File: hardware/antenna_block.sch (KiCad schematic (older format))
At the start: 28 parts

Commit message: added rx/tx wm8731 (adc/dac)
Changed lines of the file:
@@
 	2950 3100 3050 3100
 Wire Wire Line
-	3250 3100 3500 3100
+	3250 3100 3400 3100
+Wire Wire Line
+	3400 3100 3500 3100
 Wire Wire Line
 	3400 3100 3400 3200
 Connection ~ 3400 3100
 Wire Wire Line
-	3700 3100 3900 3100
+	3700 3100 3800 3100
+Wire Wire Line
+	3800 3100 3900 3100
 Wire Wire Line
 	3800 3200 3800 3100
@@
 	3400 3400 3400 3550
 Wire Wire Line
-	2600 3550 4200 3550
+	2600 3550 3400 3550
+Wire Wire Line
+	3400 3550 3800 3550
+Wire Wire Line
+	3800 3550 4200 3550
 Wire Wire Line
 	3800 3550 3800 3400
@@
 Connection ~ 3400 3550
 Wire Wire Line
-	4100 3100 4350 3100
+	4100 3100 4200 3100
+Wire Wire Line
+	4200 3100 4350 3100
 Wire Wire Line
 	4200 3100 4200 3200
@@
 	4400 3900 4400 4100
 Wire Wire Line
-	4400 3900 4650 3900
+	4400 3900 4550 3900
+Wire Wire Line
+	4550 3900 4650 3900
 Wire Wire Line
 	4550 3900 4550 4550
@@
 	5950 3850 5650 3850
 Wire Wire Line
-	5650 3650 5650 3900
+	5650 3650 5650 3850
+Wire Wire Line
+	5650 3850 5650 3900
 Connection ~ 4550 3900
 Connection ~ 5650 3850
@@
 	4650 3900 4650 3650
 Wire Wire Line
-	4950 3650 4950 3900
-Wire Wire Line
-	5350 3650 5350 3900
+	4950 3650 4950 3700
+Wire Wire Line
+	4950 3700 4950 3900
+Wire Wire Line
+	5350 3650 5350 3800
+Wire Wire Line
+	5350 3800 5350 3900
 Wire Wire Line
 	4650 4100 4650 4200
 Wire Wire Line
-	4650 4200 5650 4200
+	4650 4200 4950 4200
+Wire Wire Line
+	4950 4200 5150 4200
+Wire Wire Line
+	5150 4200 5350 4200
+Wire Wire Line
+	5350 4200 5650 4200
 Wire Wire Line
 	5650 4200 5650 4100
@@
 $EndComp
 Wire Wire Line
-	5650 3100 7750 3100
+	5650 3100 7200 3100
+Wire Wire Line
+	7200 3100 7400 3100
+Wire Wire Line
+	7400 3100 7750 3100
 Connection ~ 7200 3100
 Connection ~ 7400 3100
 Wire Wire Line
-	7950 3100 8150 3100
+	7950 3100 8050 3100
+Wire Wire Line
+	8050 3100 8150 3100
 Wire Wire Line
 	8050 3050 8050 3100
@@
 	7200 3450 7200 3300
 Wire Wire Line
-	6850 3450 7400 3450
+	6850 3450 6900 3450
+Wire Wire Line
+	6900 3450 7200 3450
+Wire Wire Line
+	7200 3450 7400 3450
 Connection ~ 7200 3450
 Connection ~ 6900 3450
@@
 	7800 3350 7800 3750
 Wire Wire Line
-	7800 3750 6900 3750
+	7800 3750 7400 3750
+Wire Wire Line
+	7400 3750 7200 3750
+Wire Wire Line
+	7200 3750 6900 3750
 Wire Wire Line
 	7400 3750 7400 3650

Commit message: Added TX chain schematic block and Vin netlist for input power_flag
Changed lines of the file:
@@
 $Descr A4 11693 8268
 encoding utf-8
-Sheet 3 4
+Sheet 3 5
 Title "Antenna block, SWR-meter and RXTX switch"
 Date "2016-09-22"
@@
 	2950 3100 3050 3100
 Wire Wire Line
-	3250 3100 3400 3100
-Wire Wire Line
-	3400 3100 3500 3100
+	3250 3100 3500 3100
 Wire Wire Line
 	3400 3100 3400 3200
 Connection ~ 3400 3100
 Wire Wire Line
-	3700 3100 3800 3100
-Wire Wire Line
-	3800 3100 3900 3100
+	3700 3100 3900 3100
 Wire Wire Line
 	3800 3200 3800 3100
@@
 	3400 3400 3400 3550
 Wire Wire Line
-	2600 3550 3400 3550
-Wire Wire Line
-	3400 3550 3800 3550
-Wire Wire Line
-	3800 3550 4200 3550
+	2600 3550 4200 3550
 Wire Wire Line
 	3800 3550 3800 3400
@@
 Connection ~ 3400 3550
 Wire Wire Line
-	4100 3100 4200 3100
-Wire Wire Line
-	4200 3100 4350 3100
+	4100 3100 4350 3100
 Wire Wire Line
 	4200 3100 4200 3200
@@
 	4400 3900 4400 4100
 Wire Wire Line
-	4400 3900 4550 3900
-Wire Wire Line
-	4550 3900 4650 3900
+	4400 3900 4650 3900
 Wire Wire Line
 	4550 3900 4550 4550
@@
 	5950 3850 5650 3850
 Wire Wire Line
-	5650 3650 5650 3850
-Wire Wire Line
-	5650 3850 5650 3900
+	5650 3650 5650 3900
 Connection ~ 4550 3900
 Connection ~ 5650 3850
@@
 	4650 3900 4650 3650
 Wire Wire Line
-	4950 3650 4950 3700
-Wire Wire Line
-	4950 3700 4950 3900
-Wire Wire Line
-	5350 3650 5350 3800
-Wire Wire Line
-	5350 3800 5350 3900
+	4950 3650 4950 3900
+Wire Wire Line
+	5350 3650 5350 3900
 Wire Wire Line
 	4650 4100 4650 4200
 Wire Wire Line
-	4650 4200 4950 4200
-Wire Wire Line
-	4950 4200 5150 4200
-Wire Wire Line
-	5150 4200 5350 4200
-Wire Wire Line
-	5350 4200 5650 4200
+	4650 4200 5650 4200
 Wire Wire Line
 	5650 4200 5650 4100
@@
 $EndComp
 Wire Wire Line
-	5650 3100 7200 3100
-Wire Wire Line
-	7200 3100 7400 3100
-Wire Wire Line
-	7400 3100 7750 3100
+	5650 3100 7750 3100
 Connection ~ 7200 3100
 Connection ~ 7400 3100
 Wire Wire Line
-	7950 3100 8050 3100
-Wire Wire Line
-	8050 3100 8150 3100
+	7950 3100 8150 3100
 Wire Wire Line
 	8050 3050 8050 3100
@@
 	7200 3450 7200 3300
 Wire Wire Line
-	6850 3450 6900 3450
-Wire Wire Line
-	6900 3450 7200 3450
-Wire Wire Line
-	7200 3450 7400 3450
+	6850 3450 7400 3450
 Connection ~ 7200 3450
 Connection ~ 6900 3450
@@
 	7400 3350 7800 3350
 Wire Wire Line
-	7800 3350 7800 3750
-Wire Wire Line
-	7800 3750 7400 3750
-Wire Wire Line
-	7400 3750 7200 3750
-Wire Wire Line
-	7200 3750 6900 3750
+	7800 3750 7800 3350
+Wire Wire Line
+	6900 3750 7800 3750
 Wire Wire Line
 	7400 3750 7400 3650

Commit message: Added RX chain. also modified and cleand up other schemas
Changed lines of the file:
@@
 $Descr A4 11693 8268
 encoding utf-8
-Sheet 3 5
+Sheet 3 7
 Title "Antenna block, SWR-meter and RXTX switch"
 Date "2016-09-22"
@@
 $EndComp
 $Comp
-L GND #PWR?
+L GND #PWR09
 U 1 1 57E329F5
 P 3800 3550
-F 0 "#PWR?" H 3800 3300 50  0001 C CNN
+F 0 "#PWR09" H 3800 3300 50  0001 C CNN
 F 1 "GND" H 3800 3400 50  0000 C CNN
 F 2 "" H 3800 3550 50  0000 C CNN
@@
 $EndComp
 $Comp
-L +Vlogic #PWR?
+L +Vlogic #PWR010
 U 1 1 57E32A6B
 P 4100 3900
-F 0 "#PWR?" H 4100 3700 50  0001 C CNN
+F 0 "#PWR010" H 4100 3700 50  0001 C CNN
 F 1 "+Vlogic" H 4100 4100 50  0000 C CNN
 F 2 "" H 4100 3900 50  0000 C CNN
@@
 $EndComp
 $Comp
-L GND #PWR?
+L GND #PWR011
 U 1 1 57E32A71
 P 5150 4300
-F 0 "#PWR?" H 5150 4050 50  0001 C CNN
+F 0 "#PWR011" H 5150 4050 50  0001 C CNN
 F 1 "GND" H 5150 4150 50  0000 C CNN
 F 2 "" H 5150 4300 50  0000 C CNN
@@
 Connection ~ 5350 3800
 $Comp
-L GND #PWR?
+L GND #PWR012
 U 1 1 57E32AAA
 P 4400 4400
-F 0 "#PWR?" H 4400 4150 50  0001 C CNN
+F 0 "#PWR012" H 4400 4150 50  0001 C CNN
 F 1 "GND" H 4400 4250 50  0000 C CNN
 F 2 "" H 4400 4400 50  0000 C CNN
@@
 Connection ~ 6900 3450
 $Comp
-L GND #PWR?
+L GND #PWR013
 U 1 1 57E32AFA
 P 7800 3750
-F 0 "#PWR?" H 7800 3500 50  0001 C CNN
+F 0 "#PWR013" H 7800 3500 50  0001 C CNN
 F 1 "GND" H 7800 3600 50  0000 C CNN
 F 2 "" H 7800 3750 50  0000 C CNN
@@
 	7400 3350 7800 3350
 Wire Wire Line
-	7800 3750 7800 3350
-Wire Wire Line
-	6900 3750 7800 3750
+	7800 3350 7800 3750
+Wire Wire Line
+	7800 3750 6900 3750
 Wire Wire Line
 	7400 3750 7400 3650

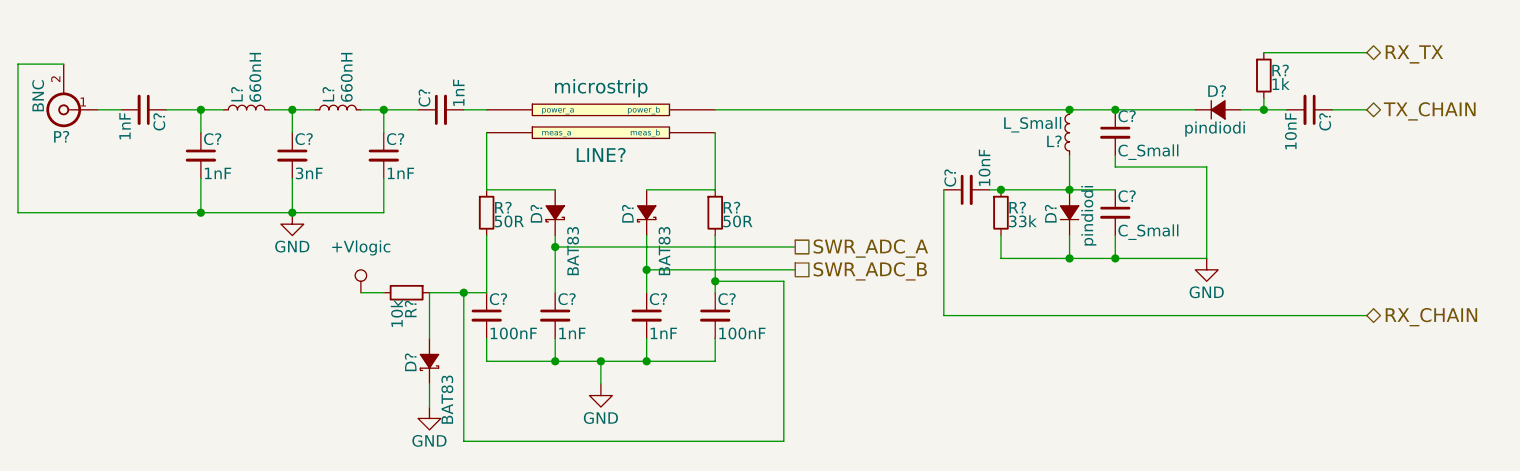
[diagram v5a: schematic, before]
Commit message: defined more component values
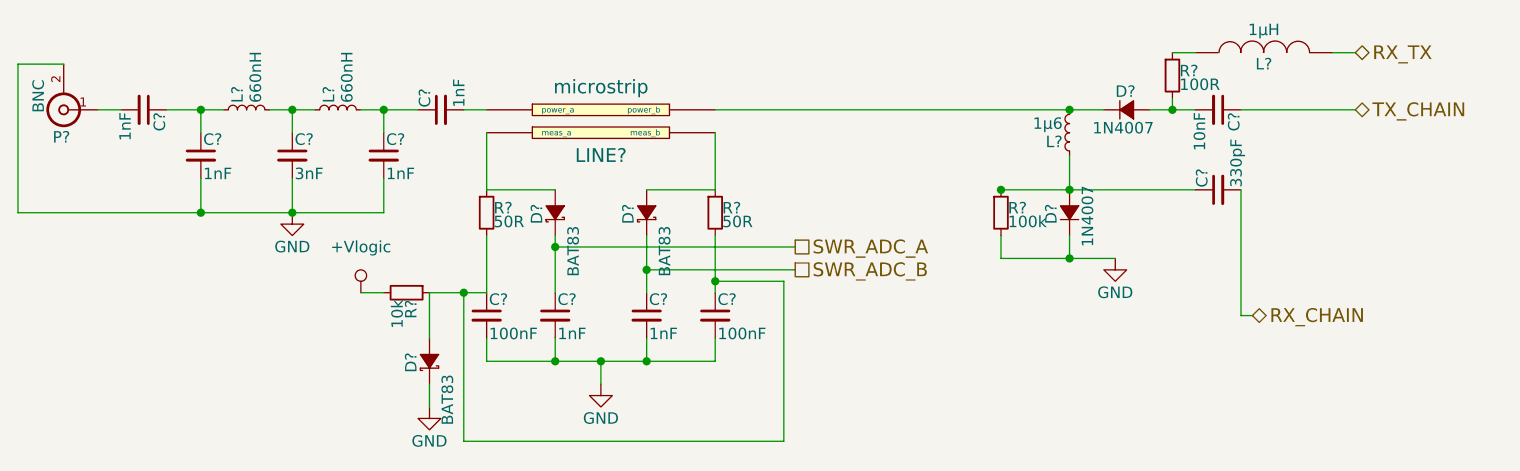
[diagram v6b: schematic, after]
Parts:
- removed C? (x2): C_Small, symbol C_Small
- added L?: 1µH, symbol INDUCTOR
- C?: value 10nF -> 330pF
- D? (x2): value pindiodi -> 1N4007
- L?: value L_Small -> 1µ6
- R?: value 33k -> 100k
- R?: value 1k -> 100R
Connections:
- net RX_CHAIN: now also C?.2; no longer C?.1
- net RX_TX: now also L?.2; no longer R?.1
- net at D?.2 (A), L?.1, R?.1: now also C?.1; no longer C?.2
- new net: L?.1, R?.1
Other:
- moved on the sheet: C?, D?, R?
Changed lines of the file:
@@
 P 7200 3200
 F 0 "L?" H 7230 3240 50  0000 L CNN
-F 1 "L_Small" H 7230 3160 50  0000 L CNN
+F 1 "1µ6" H 7230 3160 50  0000 L CNN
 F 2 "" H 7200 3200 50  0000 C CNN
 F 3 "" H 7200 3200 50  0000 C CNN
@@
 $EndComp
 $Comp
-L C_Small C?
-U 1 1 57E32AB8
-P 7400 3200
-F 0 "C?" H 7410 3270 50  0000 L CNN
-F 1 "C_Small" H 7410 3120 50  0000 L CNN
-F 2 "" H 7400 3200 50  0000 C CNN
-F 3 "" H 7400 3200 50  0000 C CNN
-	1    7400 3200
-	1    0    0    -1
-$EndComp
-$Comp
-L C_Small C?
-U 1 1 57E32ABF
-P 7400 3550
-F 0 "C?" H 7410 3620 50  0000 L CNN
-F 1 "C_Small" H 7410 3470 50  0000 L CNN
-F 2 "" H 7400 3550 50  0000 C CNN
-F 3 "" H 7400 3550 50  0000 C CNN
-	1    7400 3550
-	1    0    0    -1
-$EndComp
-$Comp
 L D_Small D?
 U 1 1 57E32AC6
 P 7200 3550
 F 0 "D?" H 7150 3630 50  0000 L CNN
-F 1 "pindiodi" H 7050 3470 50  0000 L CNN
+F 1 "1N4007" H 7050 3470 50  0000 L CNN
 F 2 "" V 7200 3550 50  0000 C CNN
 F 3 "" V 7200 3550 50  0000 C CNN
@@
 P 6900 3550
 F 0 "R?" H 6930 3570 50  0000 L CNN
-F 1 "33k" H 6930 3510 50  0000 L CNN
+F 1 "100k" H 6930 3510 50  0000 L CNN
 F 2 "" H 6900 3550 50  0000 C CNN
 F 3 "" H 6900 3550 50  0000 C CNN
@@
 L C_Small C?
 U 1 1 57E32AD4
-P 6750 3450
-F 0 "C?" H 6760 3520 50  0000 L CNN
-F 1 "10nF" H 6760 3370 50  0000 L CNN
-F 2 "" H 6750 3450 50  0000 C CNN
-F 3 "" H 6750 3450 50  0000 C CNN
-	1    6750 3450
+P 7850 3450
+F 0 "C?" H 7860 3520 50  0000 L CNN
+F 1 "330pF" H 7860 3370 50  0000 L CNN
+F 2 "" H 7850 3450 50  0000 C CNN
+F 3 "" H 7850 3450 50  0000 C CNN
+	1    7850 3450
 	0    -1   -1   0
 $EndComp
@@
 L D_Small D?
 U 1 1 57E32ADB
-P 7850 3100
-F 0 "D?" H 7800 3180 50  0000 L CNN
-F 1 "pindiodi" H 7700 3020 50  0000 L CNN
-F 2 "" V 7850 3100 50  0000 C CNN
-F 3 "" V 7850 3100 50  0000 C CNN
-	1    7850 3100
+P 7450 3100
+F 0 "D?" H 7400 3180 50  0000 L CNN
+F 1 "1N4007" H 7300 3020 50  0000 L CNN
+F 2 "" V 7450 3100 50  0000 C CNN
+F 3 "" V 7450 3100 50  0000 C CNN
+	1    7450 3100
 	1    0    0    -1
 $EndComp
@@
 L R_Small R?
 U 1 1 57E32AE2
-P 8050 2950
-F 0 "R?" H 8080 2970 50  0000 L CNN
-F 1 "1k" H 8080 2910 50  0000 L CNN
-F 2 "" H 8050 2950 50  0000 C CNN
-F 3 "" H 8050 2950 50  0000 C CNN
-	1    8050 2950
+P 7650 2950
+F 0 "R?" H 7680 2970 50  0000 L CNN
+F 1 "100R" H 7680 2910 50  0000 L CNN
+F 2 "" H 7650 2950 50  0000 C CNN
+F 3 "" H 7650 2950 50  0000 C CNN
+	1    7650 2950
 	1    0    0    -1
 $EndComp
@@
 L C_Small C?
 U 1 1 57E32AE9
-P 8250 3100
-F 0 "C?" H 8260 3170 50  0000 L CNN
-F 1 "10nF" H 8260 3020 50  0000 L CNN
-F 2 "" H 8250 3100 50  0000 C CNN
-F 3 "" H 8250 3100 50  0000 C CNN
-	1    8250 3100
+P 7850 3100
+F 0 "C?" H 7860 3170 50  0000 L CNN
+F 1 "10nF" H 7860 3020 50  0000 L CNN
+F 2 "" H 7850 3100 50  0000 C CNN
+F 3 "" H 7850 3100 50  0000 C CNN
+	1    7850 3100
 	0    1    1    0
 $EndComp
 Wire Wire Line
-	5650 3100 7750 3100
+	5650 3100 7350 3100
 Connection ~ 7200 3100
-Connection ~ 7400 3100
 Wire Wire Line
-	7950 3100 8150 3100
+	7550 3100 7750 3100
 Wire Wire Line
-	8050 3050 8050 3100
-Connection ~ 8050 3100
+	7650 3050 7650 3100
+Connection ~ 7650 3100
 Wire Wire Line
 	7200 3450 7200 3300
 Wire Wire Line
-	6850 3450 7400 3450
+	6900 3450 7750 3450
 Connection ~ 7200 3450
 Connection ~ 6900 3450
@@
 L GND #PWR013
 U 1 1 57E32AFA
-P 7800 3750
-F 0 "#PWR013" H 7800 3500 50  0001 C CNN
-F 1 "GND" H 7800 3600 50  0000 C CNN
-F 2 "" H 7800 3750 50  0000 C CNN
-F 3 "" H 7800 3750 50  0000 C CNN
-	1    7800 3750
+P 7400 3750
+F 0 "#PWR013" H 7400 3500 50  0001 C CNN
+F 1 "GND" H 7400 3600 50  0000 C CNN
+F 2 "" H 7400 3750 50  0000 C CNN
+F 3 "" H 7400 3750 50  0000 C CNN
+	1    7400 3750
 	1    0    0    -1
 $EndComp
 Wire Wire Line
-	7400 3300 7400 3350
+	6900 3750 7400 3750
 Wire Wire Line
-	7400 3350 7800 3350
-Wire Wire Line
-	7800 3350 7800 3750
-Wire Wire Line
-	7800 3750 6900 3750
-Wire Wire Line
-	7400 3750 7400 3650
-Wire Wire Line
-	7200 3750 7200 3650
-Connection ~ 7400 3750
+	7200 3650 7200 3750
 Wire Wire Line
 	6900 3750 6900 3650
 Connection ~ 7200 3750
-Text HLabel 8500 3100 2    60   BiDi ~ 0
+Text HLabel 8450 3100 2    60   BiDi ~ 0
 TX_CHAIN
 Wire Wire Line
-	8500 3100 8350 3100
-Text HLabel 8500 2850 2    60   BiDi ~ 0
+	8450 3100 7950 3100
+Text HLabel 8450 2850 2    60   BiDi ~ 0
 RX_TX
+Text HLabel 8000 4000 2    60   BiDi ~ 0
+RX_CHAIN
+$Comp
+L INDUCTOR L?
+U 1 1 57E72AA5
+P 8050 2850
+F 0 "L?" V 8000 2850 50  0000 C CNN
+F 1 "1µH" V 8150 2850 50  0000 C CNN
+F 2 "" H 8050 2850 50  0000 C CNN
+F 3 "" H 8050 2850 50  0000 C CNN
+	1    8050 2850
+	0    -1   -1   0
+$EndComp
 Wire Wire Line
-	8050 2850 8500 2850
-Text HLabel 8500 4000 2    60   BiDi ~ 0
-RX_CHAIN
+	7650 2850 7750 2850
 Wire Wire Line
-	6650 3450 6650 4000
+	8350 2850 8450 2850
 Wire Wire Line
-	6650 4000 8500 4000
+	7950 3450 7950 4000
+Wire Wire Line
+	7950 4000 8000 4000
 $EndSCHEMATC

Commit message: Allocated CPU some pins and made minor adjustments here and there
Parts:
- L?: value 1µH -> 10µH
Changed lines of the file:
@@
 	5150 4200 5150 4300
 Connection ~ 5150 4200
-Text HLabel 6000 3700 2    60   UnSpc ~ 0
+Text HLabel 6000 3700 2    60   Output ~ 0
 SWR_ADC_A
-Text HLabel 6000 3800 2    60   UnSpc ~ 0
+Text HLabel 6000 3800 2    60   Output ~ 0
 SWR_ADC_B
 Wire Wire Line
@@
 	6900 3750 6900 3650
 Connection ~ 7200 3750
-Text HLabel 8450 3100 2    60   BiDi ~ 0
+Text HLabel 8450 3100 2    60   Input ~ 0
 TX_CHAIN
 Wire Wire Line
 	8450 3100 7950 3100
-Text HLabel 8450 2850 2    60   BiDi ~ 0
+Text HLabel 8450 2850 2    60   Input ~ 0
 RX_TX
-Text HLabel 8000 4000 2    60   BiDi ~ 0
+Text HLabel 8000 4000 2    60   Output ~ 0
 RX_CHAIN
 $Comp
@@
 P 8050 2850
 F 0 "L?" V 8000 2850 50  0000 C CNN
-F 1 "1µH" V 8150 2850 50  0000 C CNN
+F 1 "10µH" V 8150 2850 50  0000 C CNN
 F 2 "" H 8050 2850 50  0000 C CNN
 F 3 "" H 8050 2850 50  0000 C CNN
